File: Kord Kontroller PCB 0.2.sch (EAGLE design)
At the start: 190 parts, among them IC2 74HCT1G125DBV, J1 MIDIOUTB, J2 MIDIOUTA, J3 FTSH-105-01-L-DV-KJ, Q1 32kHz, SW2 SPST_TACT-KMR2, U1 AP2112K-3.3, U2 ATSAMD51J19A-AUT, X3 microUSB

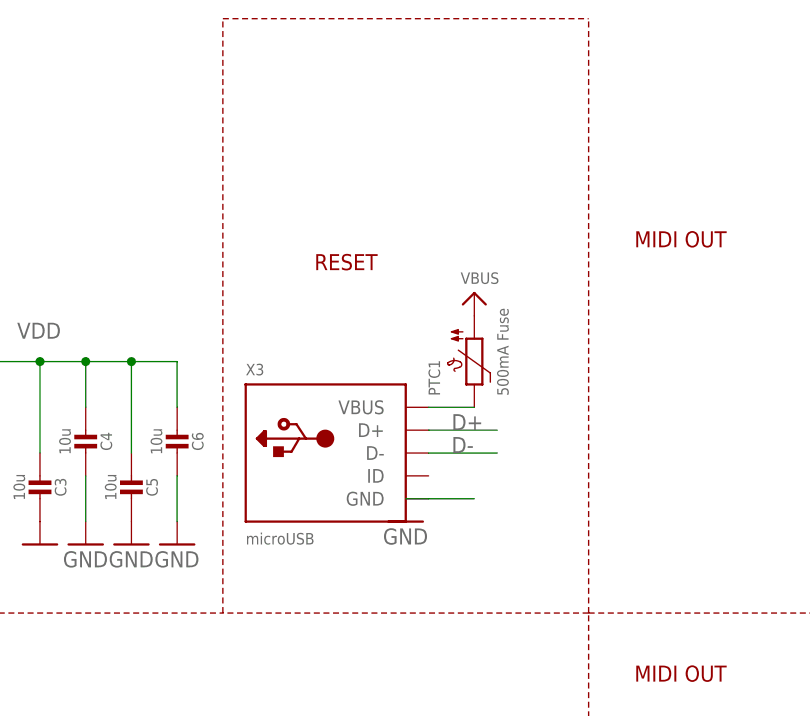
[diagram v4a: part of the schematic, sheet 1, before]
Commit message: Changed USB package and removed most of the errorsgit stash
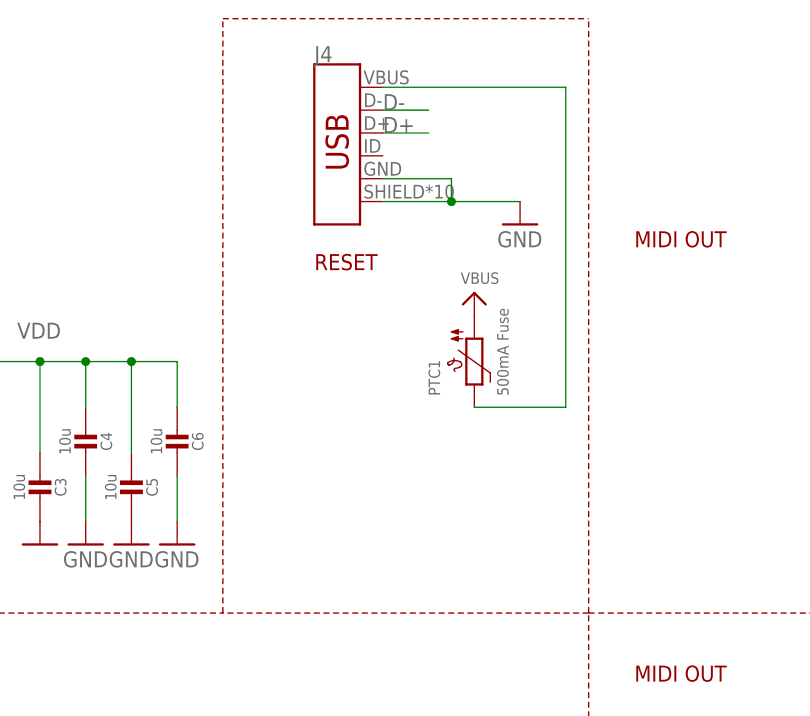
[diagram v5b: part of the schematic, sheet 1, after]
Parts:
- removed X3: microUSB, microbuilder:USB_MICRO_NARROW
- added J4: (no value), SparkFun-Connectors:USB_MICRO-B_HALF_PTH_MILL
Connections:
- net D+: now also J4.D+; no longer X3.D+
- net D-: now also J4.D-; no longer X3.D-
- net GND: now also J4.GND, J4.SHIELD; no longer X3.GND
- net N$66: now also J4.VBUS; no longer X3.VBUS
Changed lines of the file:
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@@
 <?xml version="1.0" encoding="utf-8"?>
 <!DOCTYPE eagle SYSTEM "eagle.dtd">
-<eagle version="9.2.2">
+<eagle version="9.4.2">
 <drawing>
 <settings>
@@
 <part name="U$52" library="microbuilder" deviceset="GND" device=""/>
 <part name="U$53" library="microbuilder" deviceset="GND" device=""/>
-<part name="GND14" library="supply1" deviceset="GND" device=""/>
 <part name="U$56" library="microbuilder" deviceset="VBUS" device=""/>
 <part name="U$57" library="microbuilder" deviceset="VBUS" device=""/>
-<part name="X3" library="microbuilder" deviceset="USB" device="_MICRO_NARROW" value="microUSB"/>
 <part name="U1" library="microbuilder" deviceset="VREG_SOT23-5" device="" value="AP2112K-3.3"/>
 <part name="D59" library="adafruit" deviceset="DIODE" device="_SOD-123FL" value="MBR120"/>
@@
 <part name="C8" library="microbuilder" deviceset="CAP_CERAMIC" device="0805-NOOUTLINE" value="10uF"/>
 <part name="Q1" library="special" library_urn="urn:adsk.eagle:library:367" deviceset="XTAL/S" device="" package3d_urn="urn:adsk.eagle:package:26647/2" value="32kHz"/>
+<part name="J4" library="SparkFun-Connectors" deviceset="USB_MICRO-B" device="_HALF_PTH_MILL"/>
+<part name="GND2" library="supply1" deviceset="GND" device=""/>
 </parts>
 <sheets>
@@
 <attribute name="VALUE" x="656.336" y="111.76" size="1.27" layer="96"/>
 </instance>
-<instance part="GND14" gate="1" x="754.38" y="116.84" smashed="yes">
-<attribute name="VALUE" x="751.84" y="114.3" size="1.778" layer="96"/>
-</instance>
 <instance part="U$56" gate="G$1" x="762" y="142.24" smashed="yes">
 <attribute name="VALUE" x="760.476" y="143.256" size="1.27" layer="96"/>
@@
 <instance part="U$57" gate="G$1" x="650.24" y="147.32" smashed="yes">
 <attribute name="VALUE" x="648.716" y="148.336" size="1.27" layer="96"/>
-</instance>
-<instance part="X3" gate="G$1" x="746.76" y="124.46" smashed="yes">
-<attribute name="NAME" x="736.6" y="133.096" size="1.27" layer="95"/>
-<attribute name="VALUE" x="736.6" y="114.3" size="1.27" layer="96"/>
 </instance>
 <instance part="U1" gate="G$1" x="668.02" y="132.08" smashed="yes">
@@
 <attribute name="NAME" x="651.51" y="-20.32" size="1.778" layer="95" rot="R270"/>
 <attribute name="VALUE" x="642.62" y="-20.32" size="1.778" layer="96" rot="R270"/>
+</instance>
+<instance part="J4" gate="J1" x="746.76" y="157.48" smashed="yes">
+<attribute name="VALUE" x="744.22" y="147.574" size="1.778" layer="96" font="vector" rot="MR180" align="top-left"/>
+<attribute name="NAME" x="744.22" y="167.894" size="1.778" layer="95" font="vector"/>
+</instance>
+<instance part="GND2" gate="1" x="767.08" y="149.86" smashed="yes">
+<attribute name="VALUE" x="764.54" y="147.32" size="1.778" layer="96"/>
 </instance>
 </instances>
@@
 <pinref part="U$52" gate="G$1" pin="GND"/>
 <wire x1="680.72" y1="121.92" x2="680.72" y2="116.84" width="0.1524" layer="91"/>
-</segment>
-<segment>
-<wire x1="756.92" y1="119.38" x2="762" y2="119.38" width="0.1524" layer="91"/>
-<wire x1="756.92" y1="119.38" x2="754.38" y2="119.38" width="0.1524" layer="91"/>
-<pinref part="GND14" gate="1" pin="GND"/>
-<pinref part="X3" gate="G$1" pin="GND"/>
 </segment>
 <segment>
@@
 <junction x="622.3" y="-27.94"/>
 <pinref part="C8" gate="G$1" pin="2"/>
+</segment>
+<segment>
+<pinref part="J4" gate="J1" pin="GND"/>
+<wire x1="751.84" y1="154.94" x2="759.46" y2="154.94" width="0.1524" layer="91"/>
+<wire x1="759.46" y1="154.94" x2="759.46" y2="152.4" width="0.1524" layer="91"/>
+<wire x1="767.08" y1="152.4" x2="759.46" y2="152.4" width="0.1524" layer="91"/>
+<pinref part="J4" gate="J1" pin="SHIELD"/>
+<wire x1="751.84" y1="152.4" x2="759.46" y2="152.4" width="0.1524" layer="91"/>
+<junction x="759.46" y="152.4"/>
+<pinref part="GND2" gate="1" pin="GND"/>
 </segment>
 </net>
@@
 <net name="D+" class="0">
 <segment>
-<pinref part="X3" gate="G$1" pin="D+"/>
-<wire x1="756.92" y1="127" x2="764.54" y2="127" width="0.1524" layer="91"/>
-<label x="759.46" y="127" size="1.778" layer="95"/>
-</segment>
-<segment>
 <wire x1="665.48" y1="-86.36" x2="652.78" y2="-86.36" width="0.1524" layer="91"/>
 <label x="655.32" y="-86.36" size="1.778" layer="95"/>
 <pinref part="U2" gate="G$1" pin="PA25/EIC/EXTINT[9]"/>
 </segment>
+<segment>
+<pinref part="J4" gate="J1" pin="D+"/>
+<wire x1="751.84" y1="160.02" x2="756.92" y2="160.02" width="0.1524" layer="91"/>
+<label x="751.84" y="160.02" size="1.778" layer="95"/>
+</segment>
 </net>
 <net name="D-" class="0">
-<segment>
-<pinref part="X3" gate="G$1" pin="D-"/>
-<label x="759.46" y="124.46" size="1.778" layer="95"/>
-<wire x1="764.54" y1="124.46" x2="756.92" y2="124.46" width="0.1524" layer="91"/>
-</segment>
 <segment>
 <wire x1="652.78" y1="-83.82" x2="665.48" y2="-83.82" width="0.1524" layer="91"/>
@@
 <pinref part="U2" gate="G$1" pin="PA24/EIC/EXTINT[8]"/>
 </segment>
+<segment>
+<pinref part="J4" gate="J1" pin="D-"/>
+<wire x1="751.84" y1="162.56" x2="756.92" y2="162.56" width="0.1524" layer="91"/>
+<label x="751.84" y="162.56" size="1.778" layer="95"/>
+</segment>
 </net>
 <net name="LEVELSHIFT_3V" class="0">
@@
 <net name="N$66" class="0">
 <segment>
-<wire x1="756.92" y1="129.54" x2="762" y2="129.54" width="0.1524" layer="91"/>
-<pinref part="X3" gate="G$1" pin="VBUS"/>
 <pinref part="PTC1" gate="G$1" pin="2"/>
-</segment>
-</net>
+<wire x1="762" y1="129.54" x2="772.16" y2="129.54" width="0.1524" layer="91"/>
+<pinref part="J4" gate="J1" pin="VBUS"/>
+<wire x1="751.84" y1="165.1" x2="772.16" y2="165.1" width="0.1524" layer="91"/>
+<wire x1="772.16" y1="165.1" x2="772.16" y2="129.54" width="0.1524" layer="91"/>
+</segment>
+</net>

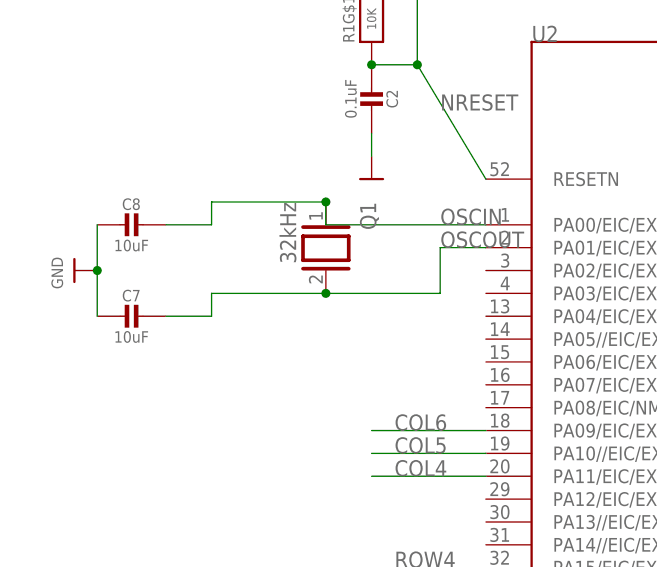
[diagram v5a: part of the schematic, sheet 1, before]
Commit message: changed crystal
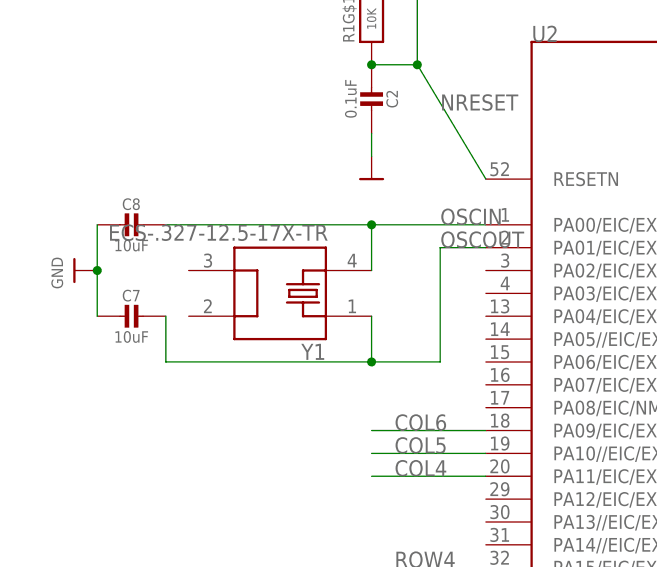
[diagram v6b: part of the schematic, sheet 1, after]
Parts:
- removed Q1: 32kHz, special:XTAL/S
- added Y1: ECS-.327-12.5-17X-TR, ECS-.327-12.5-17X-TR:ECS-.327-12.5-17X-TR
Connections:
- net OSCIN: now also Y1.4; no longer Q1.1
- net OSCOUT: now also Y1.1; no longer Q1.2
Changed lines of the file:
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@@
 <?xml version="1.0" encoding="utf-8"?>
 <!DOCTYPE eagle SYSTEM "eagle.dtd">
-<eagle version="9.4.2">
+<eagle version="9.2.2">
 <drawing>
 <settings>
@@
 <part name="C7" library="microbuilder" deviceset="CAP_CERAMIC" device="0805-NOOUTLINE" value="10uF"/>
 <part name="C8" library="microbuilder" deviceset="CAP_CERAMIC" device="0805-NOOUTLINE" value="10uF"/>
-<part name="Q1" library="special" library_urn="urn:adsk.eagle:library:367" deviceset="XTAL/S" device="" package3d_urn="urn:adsk.eagle:package:26647/2" value="32kHz"/>
 <part name="J4" library="SparkFun-Connectors" deviceset="USB_MICRO-B" device="_HALF_PTH_MILL"/>
 <part name="GND2" library="supply1" deviceset="GND" device=""/>
+<part name="Y1" library="ECS-.327-12.5-17X-TR" deviceset="ECS-.327-12.5-17X-TR" device=""/>
 </parts>
 <sheets>
@@
 <attribute name="VALUE" x="626.09" y="-25.16" size="1.27" layer="96" font="vector" align="center"/>
 </instance>
-<instance part="Q1" gate="G$1" x="647.7" y="-25.4" smashed="yes" rot="R270">
-<attribute name="NAME" x="651.51" y="-20.32" size="1.778" layer="95" rot="R270"/>
-<attribute name="VALUE" x="642.62" y="-20.32" size="1.778" layer="96" rot="R270"/>
-</instance>
 <instance part="J4" gate="J1" x="746.76" y="157.48" smashed="yes">
 <attribute name="VALUE" x="744.22" y="147.574" size="1.778" layer="96" font="vector" rot="MR180" align="top-left"/>
@@
 <instance part="GND2" gate="1" x="767.08" y="149.86" smashed="yes">
 <attribute name="VALUE" x="764.54" y="147.32" size="1.778" layer="96"/>
+</instance>
+<instance part="Y1" gate="G$1" x="642.62" y="-30.48" smashed="yes" rot="R180">
+<attribute name="NAME" x="647.71686875" y="-36.086559375" size="1.783909375" layer="95" rot="R180"/>
+<attribute name="VALUE" x="647.964559375" y="-22.84491875" size="1.78151875" layer="96" rot="R180"/>
 </instance>
 </instances>
@@
 <net name="OSCIN" class="0">
 <segment>
+<label x="660.4" y="-22.86" size="1.778" layer="95"/>
+<pinref part="C8" gate="G$1" pin="1"/>
 <pinref part="U2" gate="G$1" pin="PA00/EIC/EXTINT[0]"/>
-<label x="660.4" y="-22.86" size="1.778" layer="95"/>
-<pinref part="Q1" gate="G$1" pin="1"/>
-<wire x1="665.48" y1="-22.86" x2="647.7" y2="-22.86" width="0.1524" layer="91"/>
-<wire x1="647.7" y1="-22.86" x2="647.7" y2="-20.32" width="0.1524" layer="91"/>
-<pinref part="C8" gate="G$1" pin="1"/>
-<wire x1="629.92" y1="-22.86" x2="635" y2="-22.86" width="0.1524" layer="91"/>
-<wire x1="647.7" y1="-20.32" x2="635" y2="-20.32" width="0.1524" layer="91"/>
-<wire x1="635" y1="-20.32" x2="635" y2="-22.86" width="0.1524" layer="91"/>
-<junction x="647.7" y="-20.32"/>
+<wire x1="629.92" y1="-22.86" x2="652.78" y2="-22.86" width="0.1524" layer="91"/>
+<pinref part="Y1" gate="G$1" pin="4"/>
+<wire x1="652.78" y1="-22.86" x2="665.48" y2="-22.86" width="0.1524" layer="91"/>
+<wire x1="652.78" y1="-27.94" x2="652.78" y2="-22.86" width="0.1524" layer="91"/>
+<junction x="652.78" y="-22.86"/>
 </segment>
 </net>
@@
 <segment>
 <pinref part="U2" gate="G$1" pin="PA01/EIC/EXTINT[1]"/>
-<wire x1="660.4" y1="-30.48" x2="660.4" y2="-25.4" width="0.1524" layer="91"/>
 <wire x1="660.4" y1="-25.4" x2="665.48" y2="-25.4" width="0.1524" layer="91"/>
 <label x="660.4" y="-25.4" size="1.778" layer="95"/>
-<pinref part="Q1" gate="G$1" pin="2"/>
-<wire x1="660.4" y1="-30.48" x2="647.7" y2="-30.48" width="0.1524" layer="91"/>
+<wire x1="629.92" y1="-38.1" x2="652.78" y2="-38.1" width="0.1524" layer="91"/>
+<wire x1="652.78" y1="-38.1" x2="660.4" y2="-38.1" width="0.1524" layer="91"/>
+<wire x1="660.4" y1="-38.1" x2="660.4" y2="-25.4" width="0.1524" layer="91"/>
 <pinref part="C7" gate="G$1" pin="1"/>
-<wire x1="629.92" y1="-33.02" x2="635" y2="-33.02" width="0.1524" layer="91"/>
-<wire x1="647.7" y1="-30.48" x2="635" y2="-30.48" width="0.1524" layer="91"/>
-<wire x1="635" y1="-30.48" x2="635" y2="-33.02" width="0.1524" layer="91"/>
-<junction x="647.7" y="-30.48"/>
-</segment>
-</net>
+<wire x1="629.92" y1="-33.02" x2="629.92" y2="-38.1" width="0.1524" layer="91"/>
+<pinref part="Y1" gate="G$1" pin="1"/>
+<wire x1="652.78" y1="-33.02" x2="652.78" y2="-38.1" width="0.1524" layer="91"/>
+<junction x="652.78" y="-38.1"/>
+</segment>
+</net>
